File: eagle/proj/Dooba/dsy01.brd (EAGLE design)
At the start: 100 x 80 mm, 75 parts, among them P1 DIO, P10 SWD_CORE(SWCLK-SWDIO-GND), P11 SWD_CORE(SWCLK-SWDIO-GND), P2 CKI-CKO, P3 NOT, P4 RDY, P5 PWR(VIN-GND-RST), P6 SWD_CORE(SWCLK-SWDIO-GND), P7 SWD_CORE(SWCLK-SWDIO-GND), P8 SWD_CORE(SWCLK-SWDIO-GND), P9 SWD_CORE(SWCLK-SWDIO-GND), U1 STM32F071LQFP100, U10 S25FLXXXSSOIC16, U2 AS6C1608TSOPII-44, U3 STM32F030LQFP32, U5 STM32F030LQFP32, U6 STM32F030LQFP32, U7 STM32F030LQFP32, U8 MIC550XSOT23, U9 STM32F030LQFP32, X1 8MHz, X2 8MHz, X4 8MHz, X5 8MHz, X6 8MHz, X7 8MHz

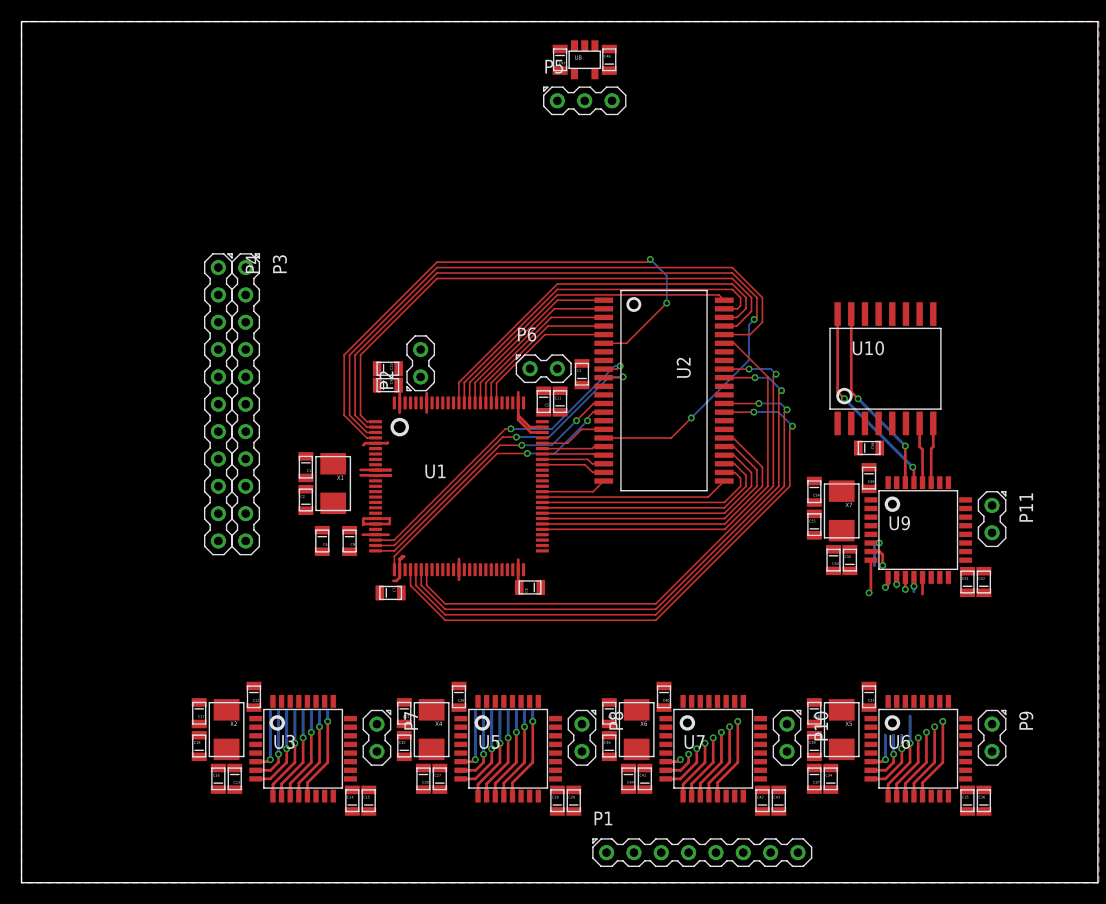
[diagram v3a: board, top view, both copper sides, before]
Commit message: Further routed DSY01
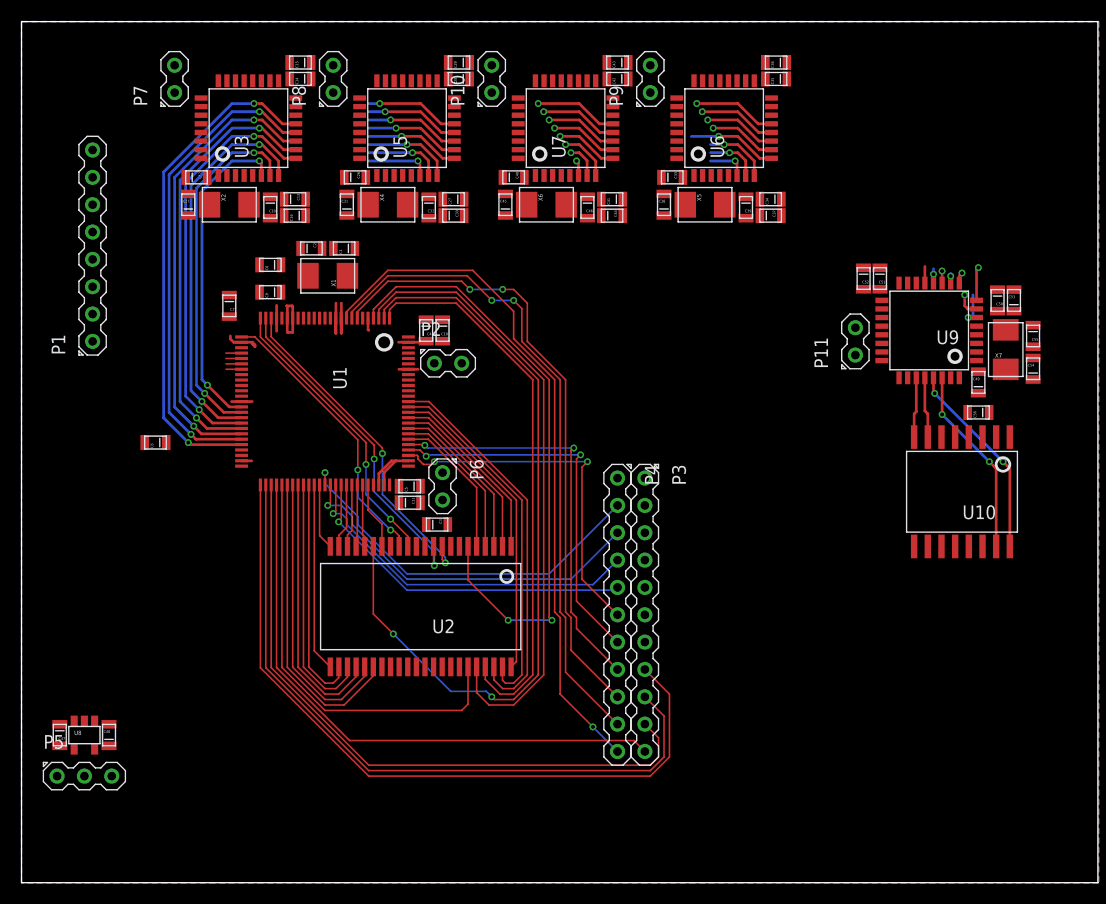
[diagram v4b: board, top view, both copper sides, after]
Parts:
- moved P1 79.9 mm to (6.60, 59.2), turned to 90 degrees
- moved C47 78.1 mm to (3.56, 13.7)
- moved C48 78.1 mm to (8.13, 13.7)
- moved P5 78.1 mm to (5.84, 9.91)
- moved U8 78.1 mm to (5.84, 13.7)
- moved C36 71.2 mm to (70.1, 76.2), turned to 0 degrees
- moved C43 70.2 mm to (55.4, 76.2), turned to 0 degrees
- moved C29 69.4 mm to (40.6, 76.2), turned to 0 degrees
- moved C35 69.4 mm to (70.1, 74.7), turned to 0 degrees
- moved P9 69.0 mm to (58.4, 74.7), turned to 90 degrees
- moved C15 68.9 mm to (25.9, 76.2), turned to 0 degrees
- moved C42 68.4 mm to (55.4, 74.7), turned to 0 degrees
- moved C28 67.7 mm to (40.6, 74.7), turned to 0 degrees
- moved C14 67.2 mm to (25.9, 74.7), turned to 0 degrees
- moved P10 67.1 mm to (43.7, 74.7), turned to 90 degrees
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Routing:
- net N$66: track 0.00 -> 69.0 mm
- net N$67: track 0.00 -> 64.8 mm
- net N$85: track 0.00 -> 64.2 mm, vias 0 -> 1
- net N$84: track 0.00 -> 61.3 mm, vias 0 -> 2
- net N$68: track 0.00 -> 60.6 mm
- net N$83: track 0.00 -> 58.4 mm, vias 0 -> 2
- net N$69: track 0.00 -> 54.4 mm
- net N$7: track 55.8 -> 1.47 mm, vias 2 -> 0
- net N$5: track 55.1 -> 1.45 mm, vias 2 -> 0
- net N$6: track 55.0 -> 1.46 mm, vias 2 -> 0
- net N$4: track 54.4 -> 1.44 mm, vias 2 -> 0
- net N$94: track 34.5 -> 72.5 mm, vias 4 -> 5
- net N$80: track 0.00 -> 38.0 mm, vias 0 -> 2
- net N$93: track 33.3 -> 69.4 mm, vias 5 -> 6
- net N$76: track 0.00 -> 35.9 mm, vias 0 -> 1
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
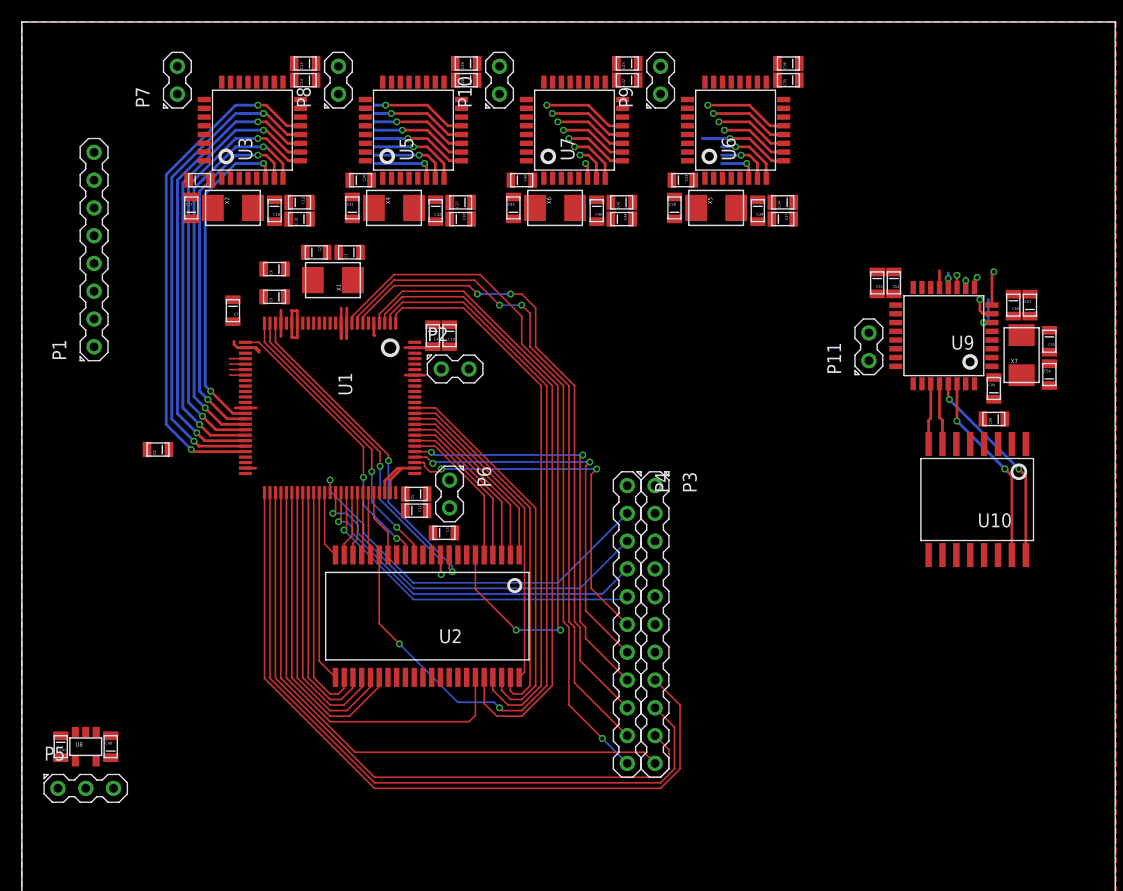
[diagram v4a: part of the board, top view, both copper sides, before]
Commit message: Further routed DSY01 board
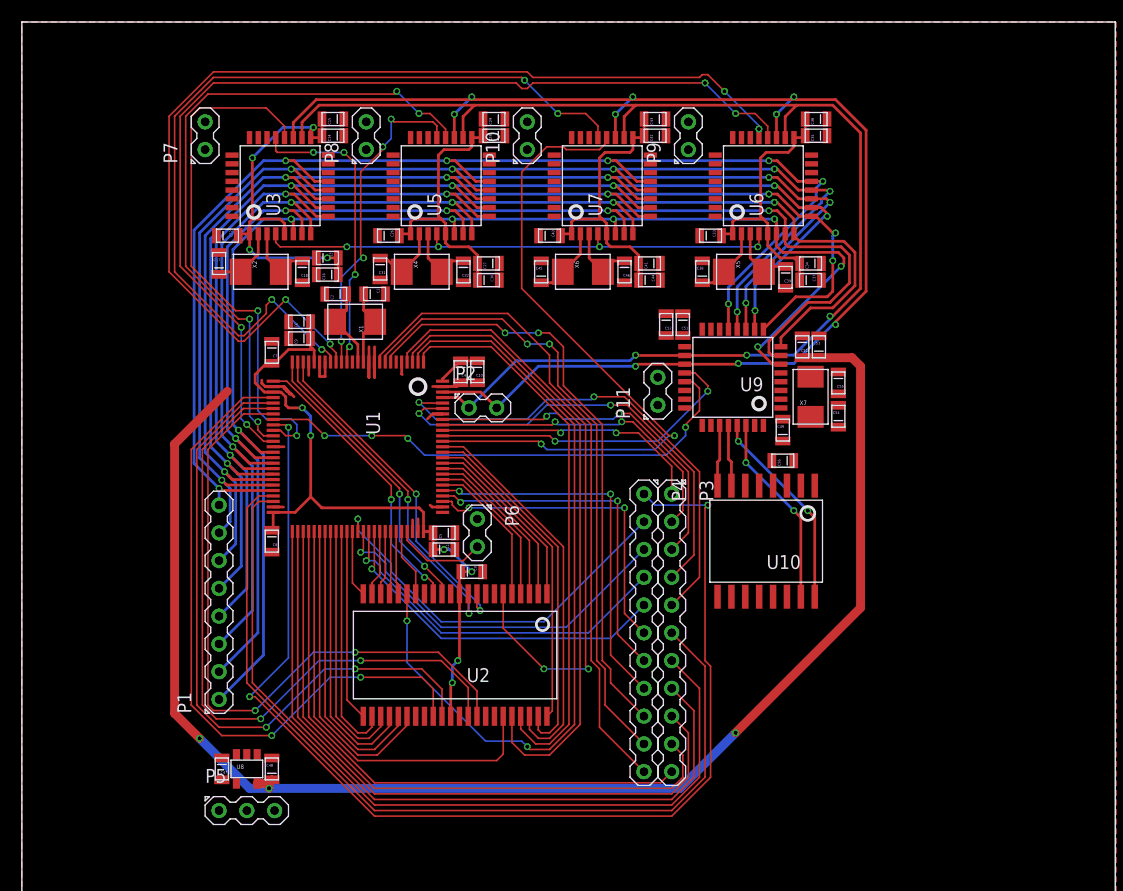
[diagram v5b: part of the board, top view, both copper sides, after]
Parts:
- moved P1 34.2 mm to (18.0, 26.9)
- moved P11 19.7 mm to (58.2, 46.2)
- moved C49 19.7 mm to (69.6, 42.7)
- moved C50 19.7 mm to (71.4, 50.3)
- moved C51 19.7 mm to (60.5, 52.3)
- moved C52 19.7 mm to (58.9, 52.3)
- moved C53 19.7 mm to (72.9, 50.3)
- moved C54 19.7 mm to (74.7, 43.9)
- moved C55 19.7 mm to (74.7, 47.0)
- moved C56 19.7 mm to (69.6, 39.9)
- moved U10 19.7 mm to (68.1, 32.5)
- moved U9 19.7 mm to (65.0, 47.5)
- moved X7 19.7 mm to (72.1, 45.7)
- moved P5 14.9 mm to (20.6, 7.87)
- moved U8 14.9 mm to (20.6, 11.7)
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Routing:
- net VCC: track 0.00 -> 314.3 mm, vias 0 -> 13
- net N$95: track 0.00 -> 128.7 mm, vias 0 -> 9
- net N$96: track 0.00 -> 121.9 mm, vias 0 -> 3
- net N$75: track 0.00 -> 107.2 mm, vias 0 -> 3
- net N$117: track 0.00 -> 95.7 mm, vias 0 -> 4
- net N$116: track 0.00 -> 91.9 mm, vias 0 -> 4
- net N$97: track 44.6 -> 126.6 mm, vias 6 -> 7
- net N$64: track 0.00 -> 81.3 mm
- net N$55: track 51.3 -> 130.8 mm, vias 6 -> 5
- net N$131: track 0.00 -> 78.5 mm, vias 0 -> 4
- net N$65: track 0.00 -> 76.4 mm
- net N$63: track 58.8 -> 129.5 mm, vias 6 -> 5
- net N$71: track 62.8 -> 128.3 mm, vias 6 -> 7
- net N$130: track 0.00 -> 61.8 mm, vias 0 -> 2
- net N$72: track 63.1 -> 124.2 mm, vias 6 -> 7
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
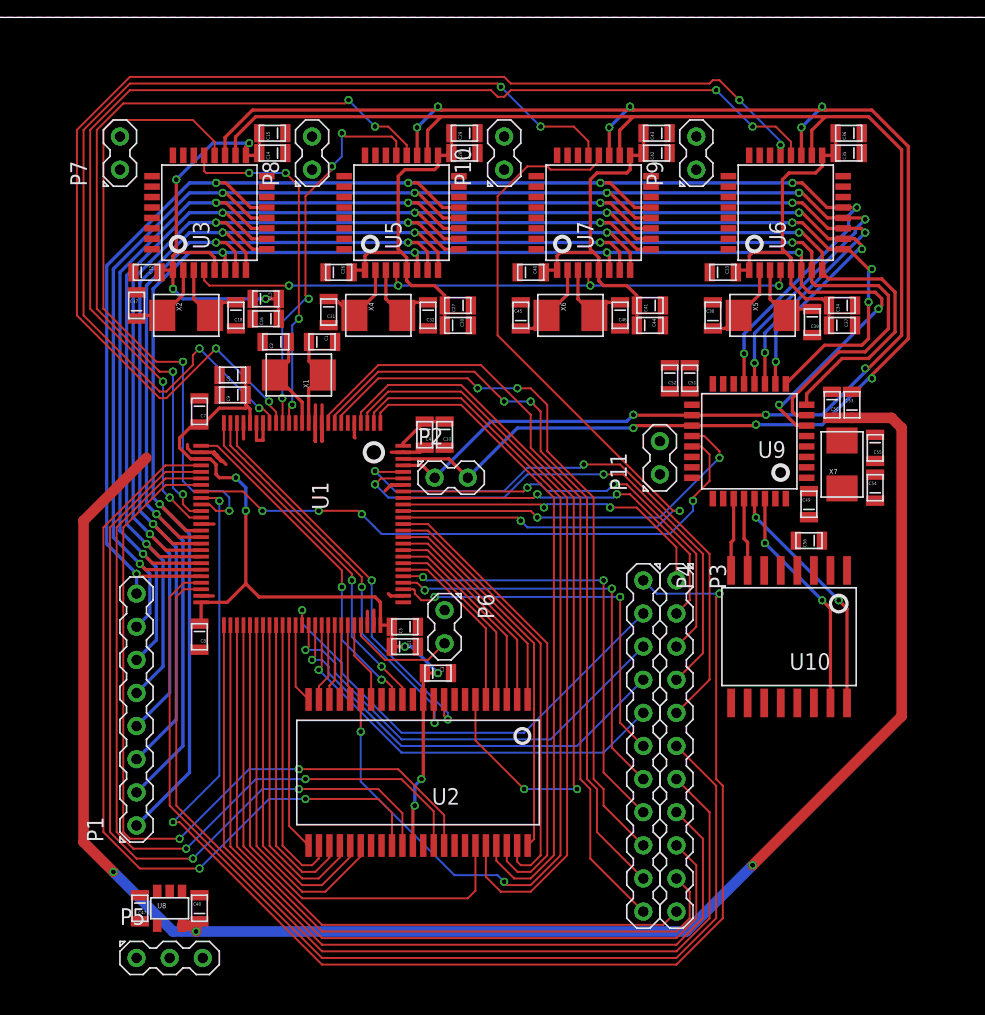
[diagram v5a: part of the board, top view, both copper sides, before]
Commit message: Routed power supply on DSY01 board
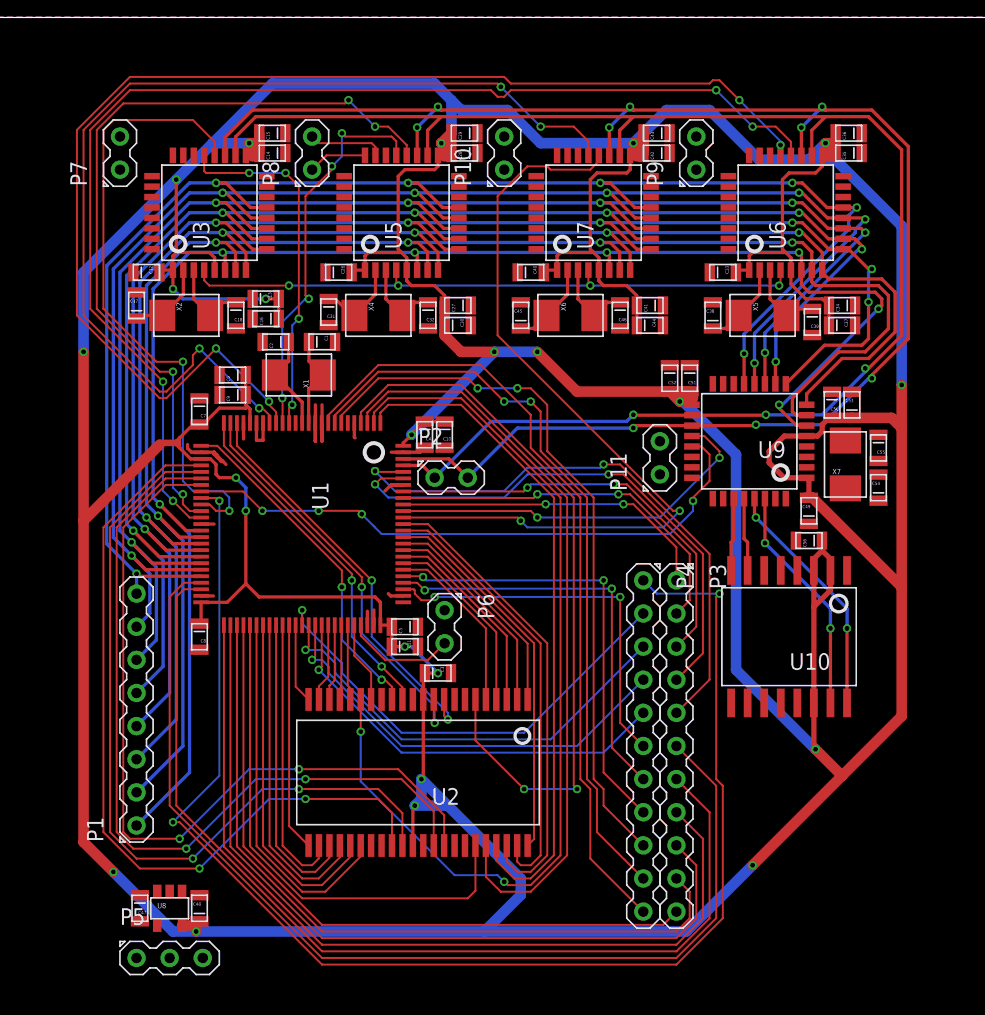
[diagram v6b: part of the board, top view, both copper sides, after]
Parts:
- moved C49 0.51 mm to (69.6, 42.2)
- moved C54 0.25 mm to (74.9, 43.9)
- moved C55 0.25 mm to (74.9, 47.0)
- moved X7 0.25 mm to (72.4, 45.7)
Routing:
- net VCC: track 314.3 -> 569.0 mm, vias 13 -> 23
- net N$46: track 0.00 -> 5.83 mm
- net N$49: track 0.00 -> 4.51 mm
- net N$72: track 124.2 -> 125.6 mm
- net N$73: track 125.5 -> 126.7 mm
- net N$93: track 123.5 -> 124.4 mm
- net N$63: track 129.5 -> 130.2 mm
- net N$71: track 128.3 -> 128.8 mm

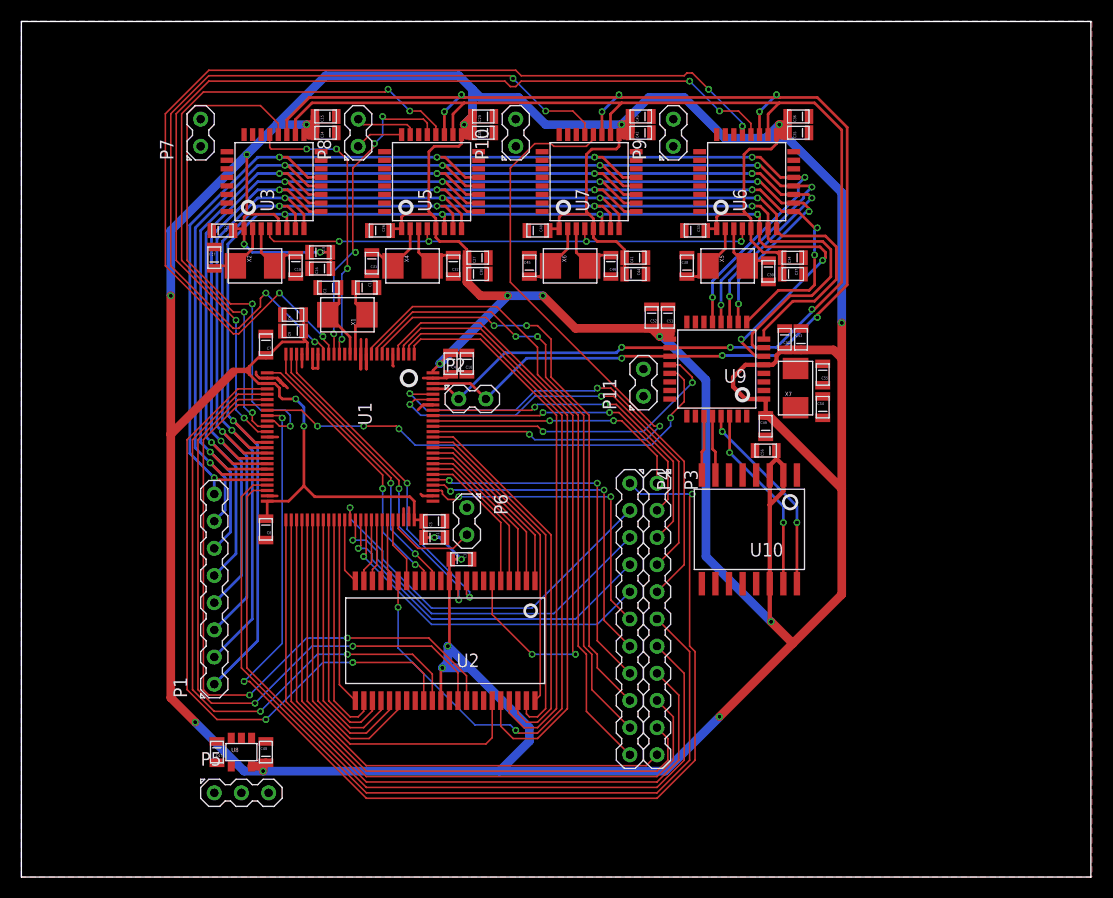
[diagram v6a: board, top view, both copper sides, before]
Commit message: Finished routing DSY01 Added LEDs on DSY01
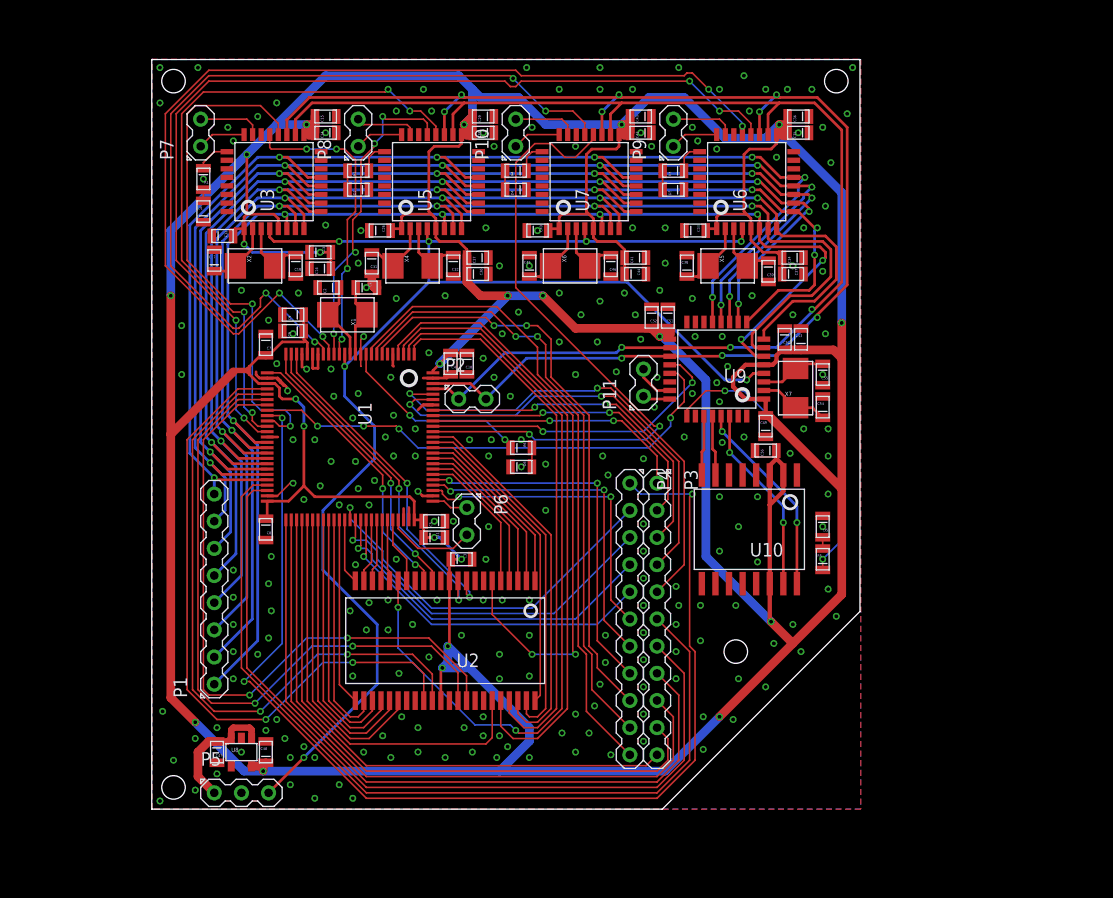
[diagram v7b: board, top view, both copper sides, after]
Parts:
- added D1, D2, D3, D4, D5, D6: LED0805, dooba:0805
- added R1, R2, R3, R4, R5, R6: 330, dooba:0805
- moved C12 0.51 mm to (18.8, 59.9)
- moved C17 0.25 mm to (18.0, 57.7)
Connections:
- new net N$109: R5.2, U9.25
- new net N$110: D6.1, R6.1
- new net N$111: R6.2, U1.10
- new net N$54: D1.1, R1.1
- new net N$56: R1.2, U3.25
- new net N$62: D2.1, R2.1
- new net N$70: R2.2, U5.25
- new net N$74: D3.1, R3.1
- new net N$87: R3.2, U6.25
- new net N$88: D4.1, R4.1
- new net N$89: R4.2, U7.25
- new net N$92: D5.1, R5.1
- net GND: now also D1.2, D2.2, D3.2, D4.2, D5.2, D6.2; no longer U1.10, U3.25, U5.25, U6.25, U7.25, U9.25
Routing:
- net N$35: track 48.8 -> 149.6 mm, vias 4 -> 7
- net N$109: track 0.00 -> 27.7 mm, vias 0 -> 2
- net N$111: track 0.00 -> 18.2 mm, vias 0 -> 2
- net N$34: track 0.00 -> 11.7 mm
- net N$98: track 0.00 -> 6.56 mm
- net N$99: track 0.00 -> 6.21 mm
- net N$42: track 0.00 -> 5.98 mm
- net N$48: track 0.00 -> 5.98 mm
- net N$50: track 0.00 -> 5.98 mm
- net N$51: track 0.00 -> 4.51 mm
- net N$47: track 0.00 -> 4.51 mm
- net N$45: track 0.00 -> 4.51 mm
- net N$52: track 0.00 -> 3.73 mm
- net N$40: track 0.00 -> 3.42 mm
- net N$56: track 0.00 -> 3.15 mm
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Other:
- board size 100 x 80 mm -> 66.2 x 70.1 mm
